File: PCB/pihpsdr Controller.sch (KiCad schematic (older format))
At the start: 16 parts, among them IC1 MCP23017T-E_SO, IC2 MCP23017T-E_SO, IC3 M24C32-RDW6TP, J3 485-1992, J6 10129379-905001BLF

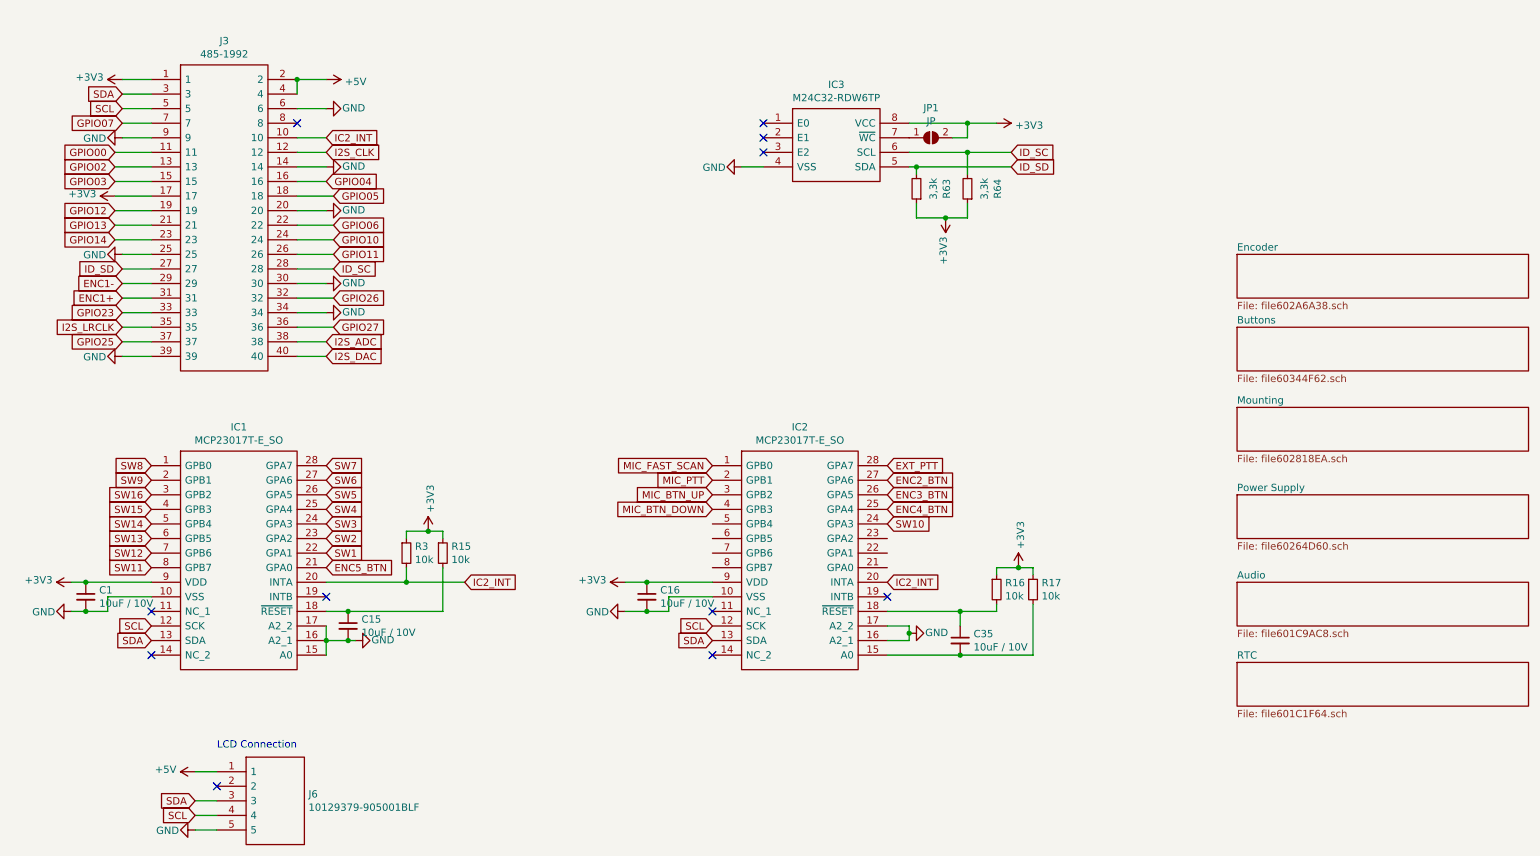
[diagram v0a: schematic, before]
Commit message: Cleaned up repository. Created a BOM in iBOM Format.
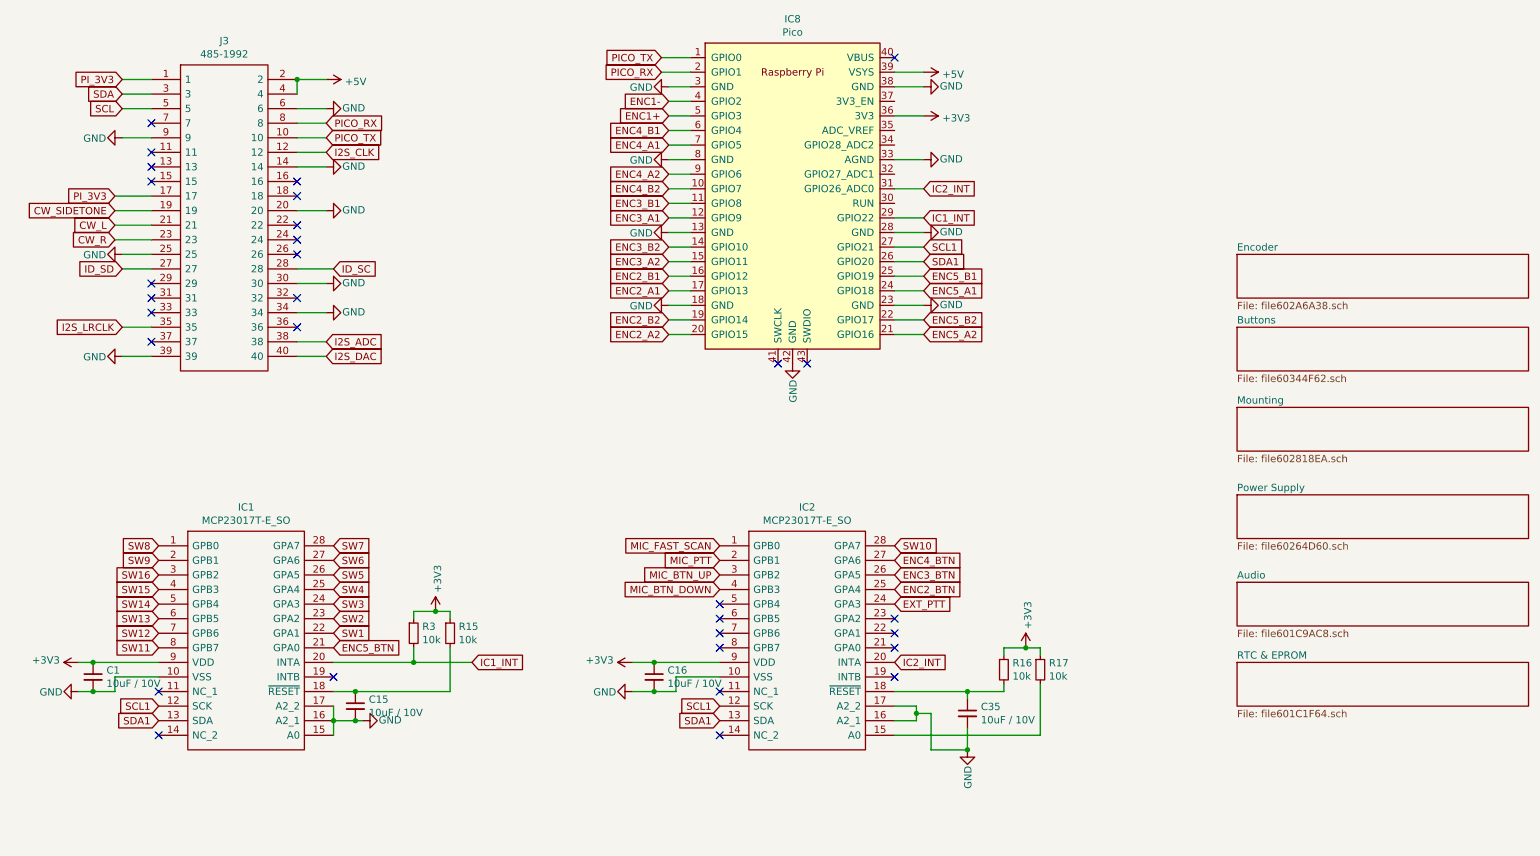
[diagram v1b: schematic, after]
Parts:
- removed IC3: M24C32-RDW6TP, SOP65P640X120-8N, symbol SamacSys_Parts:M24C32-RDW6TP
- removed J6: 10129379-905001BLF, HDRRA5W67P0X254_1X5_1270X254X241P, symbol SamacSys_Parts:10129379-905001BLF
- removed JP1: JP, Jumper:SolderJumper-2_P1.3mm_Open_RoundedPad1.0x1.5mm, symbol Jumper:SolderJumper_2_Open
- removed R63, R64: 3,3k, Resistor_SMD:R_0805_2012Metric_Pad1.15x1.40mm_HandSolder, symbol Device:R_Small
- added IC8: Pico, MCU_RaspberryPi_and_Boards:RPi_Pico_SMD_TH, symbol MCU_RaspberryPi_and_Boards:Pico
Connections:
- net +3V3: now also IC8.36 (3V3); no longer J3.1, J3.17
- net +5V: now also IC8.39 (VSYS)
- net ENC1+: now also IC8.5 (GPIO3); no longer J3.31
- net ENC1-: now also IC8.4 (GPIO2); no longer J3.29
- net ENC2_BTN: now also IC2.25 (GPA4); no longer IC2.27 (GPA6)
- net ENC4_BTN: now also IC2.27 (GPA6); no longer IC2.25 (GPA4)
- net EXT_PTT: now also IC2.24 (GPA3); no longer IC2.28 (GPA7)
- net GND: now also C35.2, IC8.13 (GND), IC8.18 (GND), IC8.23 (GND), IC8.28 (GND), IC8.3 (GND), IC8.33 (AGND), IC8.38 (GND), IC8.42 (GND), IC8.8 (GND)
- net IC2_INT: now also IC8.31 (GPIO26_ADC0); no longer IC1.20 (INTA), J3.10, R3.2
- net SCL: no longer IC1.12 (SCK), IC2.12 (SCK)
- net SDA: no longer IC1.13 (SDA), IC2.13 (SDA)
- net SW10: now also IC2.28 (GPA7); no longer IC2.24 (GPA3)
- net PICO_RX: now reaches J3.8
- net PICO_RX: now also IC8.2 (GPIO1)
- net at IC2.15 (A0), R17.2: no longer C35.2
- net GPIO00: no longer names the net of J3.11
- net GPIO02: no longer names the net of J3.13
- net GPIO03: no longer names the net of J3.15
- net GPIO04: no longer names the net of J3.16
- net GPIO05: no longer names the net of J3.18
- net GPIO06: no longer names the net of J3.22
- net GPIO07: no longer names the net of J3.7
- net GPIO10: no longer names the net of J3.24
- net GPIO11: no longer names the net of J3.26
- net GPIO12 renamed CW_SIDETONE
- net GPIO13 renamed CW_L
- net GPIO14 renamed CW_R
- net GPIO23: no longer names the net of J3.33
- net GPIO25: no longer names the net of J3.37
- net GPIO26: no longer names the net of J3.32
- net GPIO27: no longer names the net of J3.36
- new net ENC2_A1: IC8.17 (GPIO13)
- new net ENC2_A2: IC8.20 (GPIO15)
- new net ENC2_B1: IC8.16 (GPIO12)
- new net ENC2_B2: IC8.19 (GPIO14)
- new net ENC3_A1: IC8.12 (GPIO9)
- new net ENC3_A2: IC8.15 (GPIO11)
- new net ENC3_B1: IC8.11 (GPIO8)
- new net ENC3_B2: IC8.14 (GPIO10)
- new net ENC4_A1: IC8.7 (GPIO5)
- new net ENC4_A2: IC8.9 (GPIO6)
- new net ENC4_B1: IC8.6 (GPIO4)
- new net ENC4_B2: IC8.10 (GPIO7)
- new net ENC5_A1: IC8.24 (GPIO18)
- new net ENC5_A2: IC8.21 (GPIO16)
- new net ENC5_B1: IC8.25 (GPIO19)
- new net ENC5_B2: IC8.22 (GPIO17)
- new net IC1_INT: IC1.20 (INTA), IC8.29 (GPIO22), R3.2
- new net PICO_TX: IC8.1 (GPIO0), J3.10
- new net PI_3V3: J3.1, J3.17
- new net SCL1: IC1.12 (SCK), IC2.12 (SCK), IC8.27 (GPIO21)
- new net SDA1: IC1.13 (SDA), IC2.13 (SDA), IC8.26 (GPIO20)
- no-connect marks 11 -> 31
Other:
- note removed: "LCD Connection"
- moved on the sheet: C1, C15, C16, C35, IC1, IC2, R15, R16, R17, R3

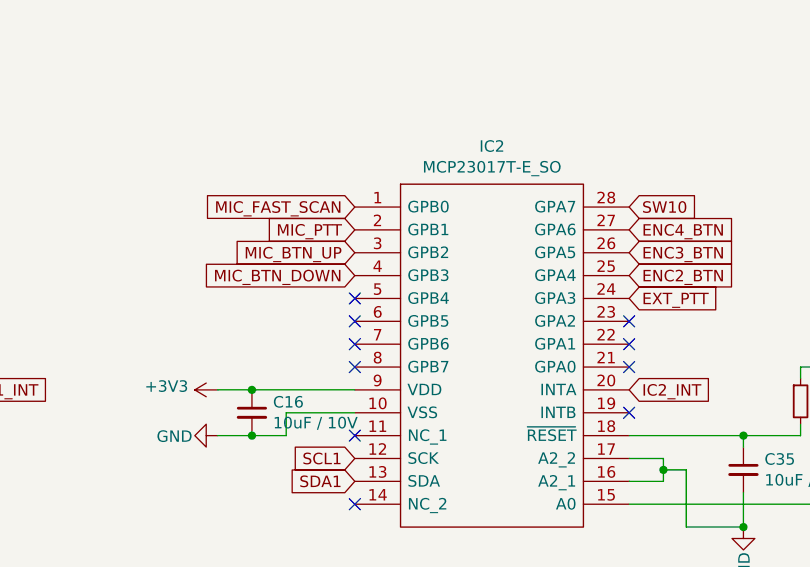
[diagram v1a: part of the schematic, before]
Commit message: Completed parts details on schematics and recreated gerbers and bom.
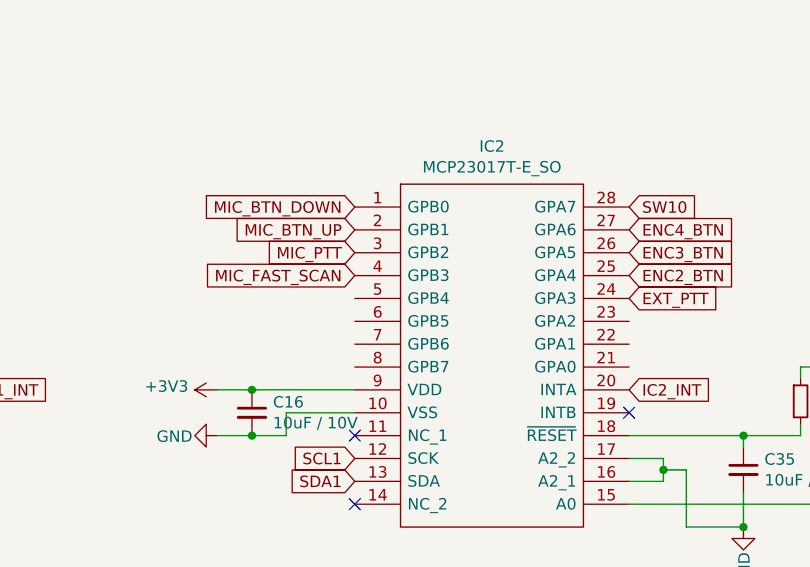
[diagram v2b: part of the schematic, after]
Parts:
- C1, C15, C16, C35: LCSC (none) -> C91245; Manufacturer_Name (none) -> Samsung Electro-Mechanics; Manufacturer_Part_Number (none) -> CL21A106MPFNNNE; Mouser Part Number (none) -> 187-CL21A106MPFNNNE
- IC1, IC2: LCSC (none) -> C47023
- IC8: Manufacturer_Name (none) -> Raspberry Pi Foundation; Manufacturer_Part_Number (none) -> DEV-17829; Mouser Part Number (none) -> 474-DEV-17829
- R15, R16, R17, R3: LCSC (none) -> C17414; Manufacturer_Name (none) -> Vishay; Manufacturer_Part_Number (none) -> CRCW080510K0FKEAC; Mouser Part Number (none) -> 71-CRCW080510K0FKEAC
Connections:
- net MIC_BTN_DOWN: now also IC2.1 (GPB0); no longer IC2.4 (GPB3)
- net MIC_BTN_UP: now also IC2.2 (GPB1); no longer IC2.3 (GPB2)
- net MIC_FAST_SCAN: now also IC2.4 (GPB3); no longer IC2.1 (GPB0)
- net MIC_PTT: now also IC2.3 (GPB2); no longer IC2.2 (GPB1)
- no-connect marks 31 -> 24
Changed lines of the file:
@@
 F 8 "Microchip" H 6300 4000 50  0001 L CNN "Manufacturer_Name"
 F 9 "MCP23017T-E/SO" H 6300 3900 50  0001 L CNN "Manufacturer_Part_Number"
+F 10 "C47023" H 5250 4500 50  0001 C CNN "LCSC"
 	1    5250 4500
 	1    0    0    -1
@@
 F 8 "Microchip" H 2450 4000 50  0001 L CNN "Manufacturer_Name"
 F 9 "MCP23017T-E/SO" H 2450 3900 50  0001 L CNN "Manufacturer_Part_Number"
+F 10 "C47023" H 1400 4500 50  0001 C CNN "LCSC"
 	1    1400 4500
 	1    0    0    -1
@@
 F 2 "Resistor_SMD:R_0805_2012Metric_Pad1.15x1.40mm_HandSolder" H 3150 5100 50  0001 C CNN
 F 3 "~" H 3150 5100 50  0001 C CNN
+F 4 "71-CRCW080510K0FKEAC" H 3150 5100 50  0001 C CNN "Mouser Part Number"
+F 5 "Vishay" H 3150 5100 50  0001 C CNN "Manufacturer_Name"
+F 6 "CRCW080510K0FKEAC" H 3150 5100 50  0001 C CNN "Manufacturer_Part_Number"
+F 7 "C17414" H 3150 5100 50  0001 C CNN "LCSC"
 	1    3150 5100
 	1    0    0    -1
 $EndComp
+Text GLabel 5250 4800 0    50   Input ~ 0
+MIC_FAST_SCAN
+Text GLabel 5250 4600 0    50   Input ~ 0
+MIC_BTN_UP
 Text GLabel 5250 4500 0    50   Input ~ 0
-MIC_FAST_SCAN
+MIC_BTN_DOWN
 Text GLabel 5250 4700 0    50   Input ~ 0
-MIC_BTN_UP
-Text GLabel 5250 4800 0    50   Input ~ 0
-MIC_BTN_DOWN
-Text GLabel 5250 4600 0    50   Input ~ 0
 MIC_PTT
 Text GLabel 6450 5300 2    50   Input ~ 0
@@
 F 2 "Resistor_SMD:R_0805_2012Metric_Pad1.15x1.40mm_HandSolder" H 7200 5350 50  0001 C CNN
 F 3 "~" H 7200 5350 50  0001 C CNN
+F 4 "C17414" H 7200 5350 50  0001 C CNN "LCSC"
+F 5 "Vishay" H 7200 5350 50  0001 C CNN "Manufacturer_Name"
+F 6 "CRCW080510K0FKEAC" H 7200 5350 50  0001 C CNN "Manufacturer_Part_Number"
+F 7 "71-CRCW080510K0FKEAC" H 7200 5350 50  0001 C CNN "Mouser Part Number"
 	1    7200 5350
 	1    0    0    -1
@@
 F 2 "Resistor_SMD:R_0805_2012Metric_Pad1.15x1.40mm_HandSolder" H 3400 5100 50  0001 C CNN
 F 3 "~" H 3400 5100 50  0001 C CNN
+F 4 "C17414" H 3400 5100 50  0001 C CNN "LCSC"
+F 5 "Vishay" H 3400 5100 50  0001 C CNN "Manufacturer_Name"
+F 6 "CRCW080510K0FKEAC" H 3400 5100 50  0001 C CNN "Manufacturer_Part_Number"
+F 7 "71-CRCW080510K0FKEAC" H 3400 5100 50  0001 C CNN "Mouser Part Number"
 	1    3400 5100
 	1    0    0    -1
@@
 F 2 "Resistor_SMD:R_0805_2012Metric_Pad1.15x1.40mm_HandSolder" H 7450 5350 50  0001 C CNN
 F 3 "~" H 7450 5350 50  0001 C CNN
+F 4 "C17414" H 7450 5350 50  0001 C CNN "LCSC"
+F 5 "Vishay" H 7450 5350 50  0001 C CNN "Manufacturer_Name"
+F 6 "CRCW080510K0FKEAC" H 7450 5350 50  0001 C CNN "Manufacturer_Part_Number"
+F 7 "71-CRCW080510K0FKEAC" H 7450 5350 50  0001 C CNN "Mouser Part Number"
 	1    7450 5350
 	1    0    0    -1
@@
 F 2 "Capacitor_SMD:C_0805_2012Metric_Pad1.15x1.40mm_HandSolder" H 950 5400 50  0001 C CNN
 F 3 "~" H 950 5400 50  0001 C CNN
+F 4 "C91245" H 950 5400 50  0001 C CNN "LCSC"
+F 5 "Samsung Electro-Mechanics" H 950 5400 50  0001 C CNN "Manufacturer_Name"
+F 6 "CL21A106MPFNNNE" H 950 5400 50  0001 C CNN "Manufacturer_Part_Number"
+F 7 "187-CL21A106MPFNNNE" H 950 5400 50  0001 C CNN "Mouser Part Number"
 	1    950  5400
 	1    0    0    -1
@@
 F 2 "Capacitor_SMD:C_0805_2012Metric_Pad1.15x1.40mm_HandSolder" H 2750 5600 50  0001 C CNN
 F 3 "~" H 2750 5600 50  0001 C CNN
+F 4 "C91245" H 2750 5600 50  0001 C CNN "LCSC"
+F 5 "Samsung Electro-Mechanics" H 2750 5600 50  0001 C CNN "Manufacturer_Name"
+F 6 "CL21A106MPFNNNE" H 2750 5600 50  0001 C CNN "Manufacturer_Part_Number"
+F 7 "187-CL21A106MPFNNNE" H 2750 5600 50  0001 C CNN "Mouser Part Number"
 	1    2750 5600
 	1    0    0    -1
@@
 F 2 "Capacitor_SMD:C_0805_2012Metric_Pad1.15x1.40mm_HandSolder" H 4800 5400 50  0001 C CNN
 F 3 "~" H 4800 5400 50  0001 C CNN
+F 4 "C91245" H 4800 5400 50  0001 C CNN "LCSC"
+F 5 "Samsung Electro-Mechanics" H 4800 5400 50  0001 C CNN "Manufacturer_Name"
+F 6 "CL21A106MPFNNNE" H 4800 5400 50  0001 C CNN "Manufacturer_Part_Number"
+F 7 "187-CL21A106MPFNNNE" H 4800 5400 50  0001 C CNN "Mouser Part Number"
 	1    4800 5400
 	1    0    0    -1
@@
 F 2 "Capacitor_SMD:C_0805_2012Metric_Pad1.15x1.40mm_HandSolder" H 6950 5650 50  0001 C CNN
 F 3 "~" H 6950 5650 50  0001 C CNN
+F 4 "C91245" H 6950 5650 50  0001 C CNN "LCSC"
+F 5 "Samsung Electro-Mechanics" H 6950 5650 50  0001 C CNN "Manufacturer_Name"
+F 6 "CL21A106MPFNNNE" H 6950 5650 50  0001 C CNN "Manufacturer_Part_Number"
+F 7 "187-CL21A106MPFNNNE" H 6950 5650 50  0001 C CNN "Mouser Part Number"
 	1    6950 5650
 	1    0    0    -1
@@
 F 2 "MCU_RaspberryPi_and_Boards:RPi_Pico_SMD_TH" V 5750 2100 50  0001 C CNN
 F 3 "" H 5750 2100 50  0001 C CNN
+F 4 "474-DEV-17829" H 5750 2100 50  0001 C CNN "Mouser Part Number"
+F 5 "Raspberry Pi Foundation" H 5750 2100 50  0001 C CNN "Manufacturer_Name"
+F 6 "DEV-17829" H 5750 2100 50  0001 C CNN "Manufacturer_Part_Number"
 	1    5750 2100
 	1    0    0    -1
@@
 NoConn ~ 2350 2100
 NoConn ~ 2350 2000
-NoConn ~ 6450 5000
-NoConn ~ 6450 5100
-NoConn ~ 6450 5200
-NoConn ~ 5250 5200
-NoConn ~ 5250 5100
-NoConn ~ 5250 5000
-NoConn ~ 5250 4900
 Wire Wire Line
 	6450 5800 7450 5800

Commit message: Refactored JLC Part Numbers. And replaced 100uF capacitors with 1206 sized parts.
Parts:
- C1, C15, C16, C35: LCSC C91245 -> C15850
- IC1, IC2: LCSC C47023 -> (none)
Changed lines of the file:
@@
 F 8 "Microchip" H 6300 4000 50  0001 L CNN "Manufacturer_Name"
 F 9 "MCP23017T-E/SO" H 6300 3900 50  0001 L CNN "Manufacturer_Part_Number"
-F 10 "C47023" H 5250 4500 50  0001 C CNN "LCSC"
+F 10 "" H 5250 4500 50  0001 C CNN "LCSC"
 	1    5250 4500
 	1    0    0    -1
@@
 F 8 "Microchip" H 2450 4000 50  0001 L CNN "Manufacturer_Name"
 F 9 "MCP23017T-E/SO" H 2450 3900 50  0001 L CNN "Manufacturer_Part_Number"
-F 10 "C47023" H 1400 4500 50  0001 C CNN "LCSC"
+F 10 "" H 1400 4500 50  0001 C CNN "LCSC"
 	1    1400 4500
 	1    0    0    -1
@@
 F 2 "Capacitor_SMD:C_0805_2012Metric_Pad1.15x1.40mm_HandSolder" H 950 5400 50  0001 C CNN
 F 3 "~" H 950 5400 50  0001 C CNN
-F 4 "C91245" H 950 5400 50  0001 C CNN "LCSC"
+F 4 "C15850" H 950 5400 50  0001 C CNN "LCSC"
 F 5 "Samsung Electro-Mechanics" H 950 5400 50  0001 C CNN "Manufacturer_Name"
 F 6 "CL21A106MPFNNNE" H 950 5400 50  0001 C CNN "Manufacturer_Part_Number"
@@
 F 2 "Capacitor_SMD:C_0805_2012Metric_Pad1.15x1.40mm_HandSolder" H 2750 5600 50  0001 C CNN
 F 3 "~" H 2750 5600 50  0001 C CNN
-F 4 "C91245" H 2750 5600 50  0001 C CNN "LCSC"
+F 4 "C15850" H 2750 5600 50  0001 C CNN "LCSC"
 F 5 "Samsung Electro-Mechanics" H 2750 5600 50  0001 C CNN "Manufacturer_Name"
 F 6 "CL21A106MPFNNNE" H 2750 5600 50  0001 C CNN "Manufacturer_Part_Number"
@@
 F 2 "Capacitor_SMD:C_0805_2012Metric_Pad1.15x1.40mm_HandSolder" H 4800 5400 50  0001 C CNN
 F 3 "~" H 4800 5400 50  0001 C CNN
-F 4 "C91245" H 4800 5400 50  0001 C CNN "LCSC"
+F 4 "C15850" H 4800 5400 50  0001 C CNN "LCSC"
 F 5 "Samsung Electro-Mechanics" H 4800 5400 50  0001 C CNN "Manufacturer_Name"
 F 6 "CL21A106MPFNNNE" H 4800 5400 50  0001 C CNN "Manufacturer_Part_Number"
@@
 F 2 "Capacitor_SMD:C_0805_2012Metric_Pad1.15x1.40mm_HandSolder" H 6950 5650 50  0001 C CNN
 F 3 "~" H 6950 5650 50  0001 C CNN
-F 4 "C91245" H 6950 5650 50  0001 C CNN "LCSC"
+F 4 "C15850" H 6950 5650 50  0001 C CNN "LCSC"
 F 5 "Samsung Electro-Mechanics" H 6950 5650 50  0001 C CNN "Manufacturer_Name"
 F 6 "CL21A106MPFNNNE" H 6950 5650 50  0001 C CNN "Manufacturer_Part_Number"

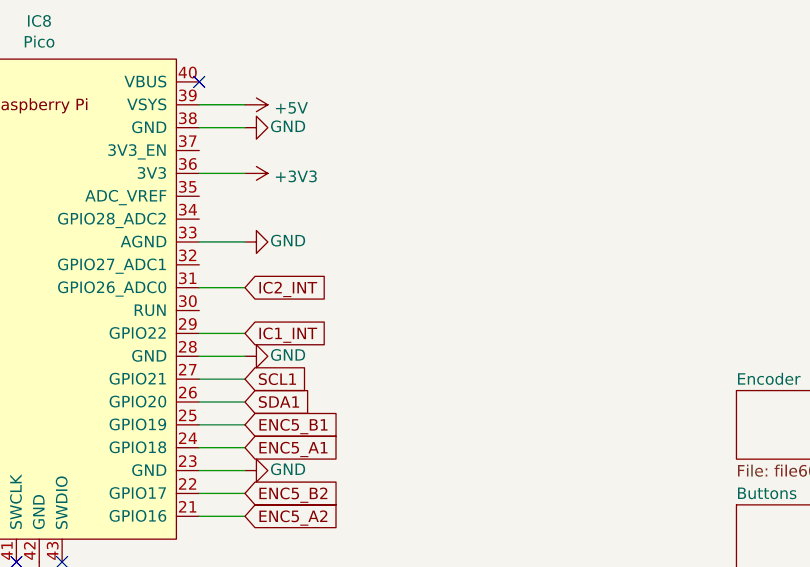
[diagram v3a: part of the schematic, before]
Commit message: Added Reset Button to Pi Pico to make updating firmware easier.
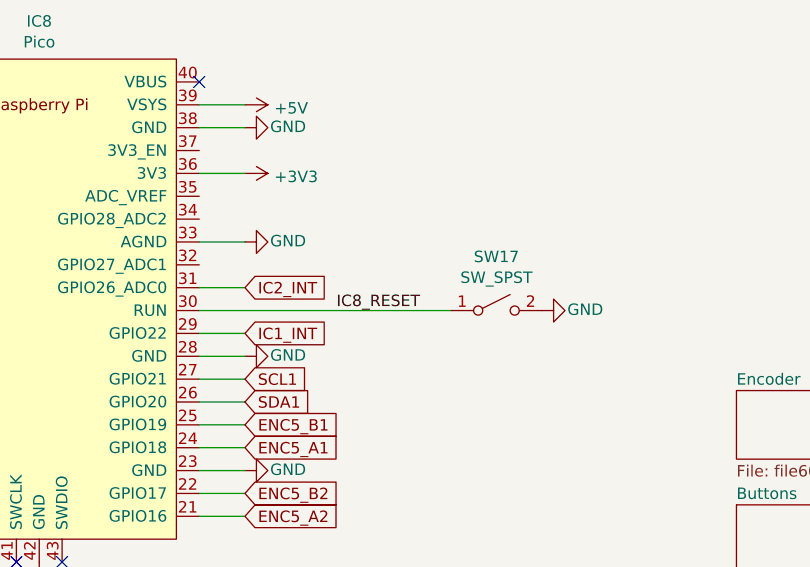
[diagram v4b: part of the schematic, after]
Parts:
- added SW17: SW_SPST, SamacSys_Parts:TL3301SPF260QG, symbol Switch:SW_SPST
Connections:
- net GND: now also SW17.2 (B)
- net IC8_RESET: now reaches IC8.30 (RUN)
- net IC8_RESET: now also SW17.1 (A)
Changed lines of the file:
@@
 	6950 5750 6950 5900
 Connection ~ 6950 5900
+$Comp
+L Switch:SW_SPST SW17
+U 1 1 603589EA
+P 7750 2150
+F 0 "SW17" H 7750 2385 50  0000 C CNN
+F 1 "SW_SPST" H 7750 2294 50  0000 C CNN
+F 2 "SamacSys_Parts:TL3301SPF260QG" H 7750 2150 50  0001 C CNN
+F 3 "~" H 7750 2150 50  0001 C CNN
+F 4 "E-Switch" H 7750 2150 50  0001 C CNN "Manufacturer_Name"
+F 5 "TL3301AF160QG" H 7750 2150 50  0001 C CNN "Manufacturer_Part_Number"
+F 6 "C273519" H 7750 2150 50  0001 C CNN "LCSC"
+	1    7750 2150
+	1    0    0    -1
+$EndComp
+$Comp
+L power:GND #PWR0126
+U 1 1 6035D907
+P 7950 2150
+F 0 "#PWR0126" H 7950 1900 50  0001 C CNN
+F 1 "GND" V 7954 2040 50  0000 R CNN
+F 2 "" H 7950 2150 50  0001 C CNN
+F 3 "" H 7950 2150 50  0001 C CNN
+	1    7950 2150
+	0    -1   -1   0
+$EndComp
+Wire Wire Line
+	6450 2150 7550 2150
+Text Label 7050 2150 0    50   ~ 0
+IC8_RESET
 $EndSCHEMATC
